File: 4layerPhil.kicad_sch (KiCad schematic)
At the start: 56 parts, among them J1 USB_C_Receptacle_USB2.0_16P, J2 Conn_01x05_Pin, J3 Conn_01x04_Pin, J4 DM3AT-SF-PEJM5, SW1 SW_SPDT, SW2 BTN1, SW3 BTN2, SW4 BTN3, U1 LM3671MF-3.3, U2 USBLC6-2SC6, U3 STM32F103RCTx, Y1 16MHz

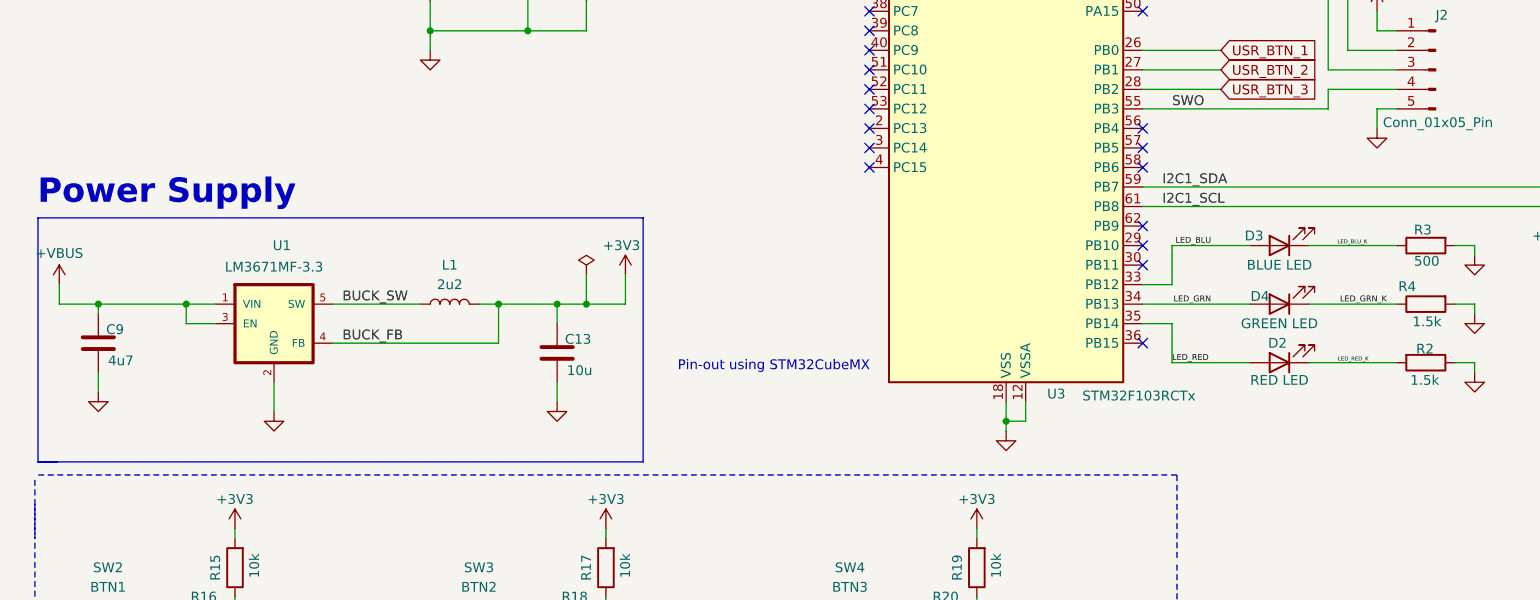
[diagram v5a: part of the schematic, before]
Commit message: Added and laid out new power supply section with new buck converter
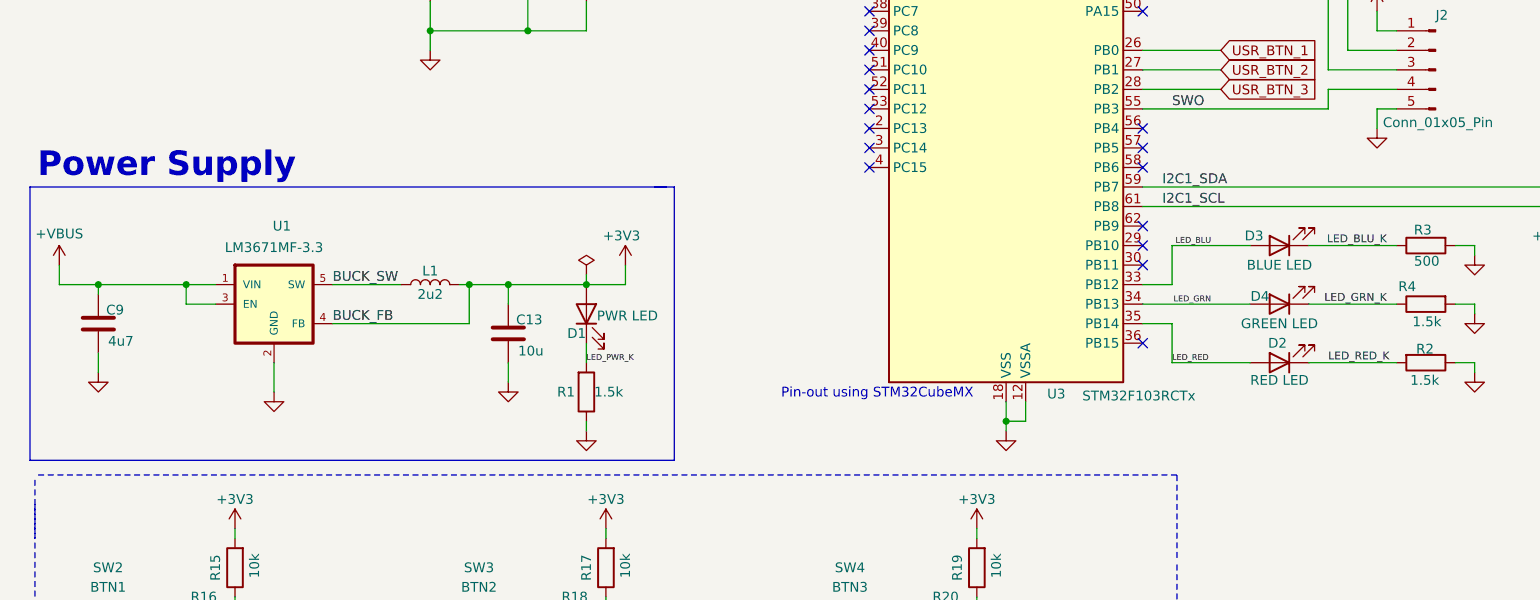
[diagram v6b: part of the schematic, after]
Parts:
- added D1: PWR LED, LED_SMD:LED_0603_1608Metric, symbol Device:LED
- added R1: 1.5k, Resistor_SMD:R_0603_1608Metric, symbol Device:R
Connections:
- net +3V3: now also D1.2 (A)
- net GND: now also R1.1
- new net LED_PWR_K: D1.1 (K), R1.2
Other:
- moved on the sheet: C13, C9, L1, U1
